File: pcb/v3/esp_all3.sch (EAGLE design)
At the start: 31 parts, among them IC1 4000D, Q1 BUZ11BH

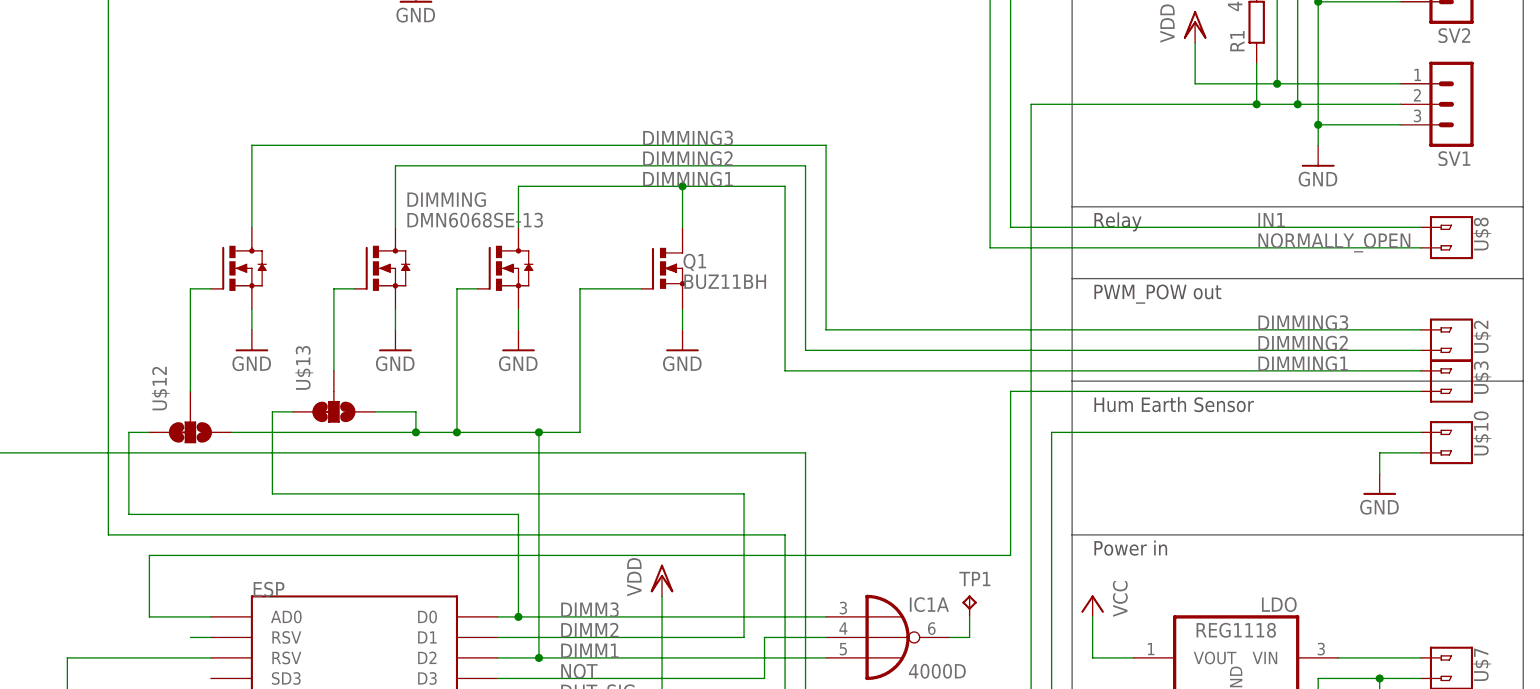
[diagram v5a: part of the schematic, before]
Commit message: added jumper
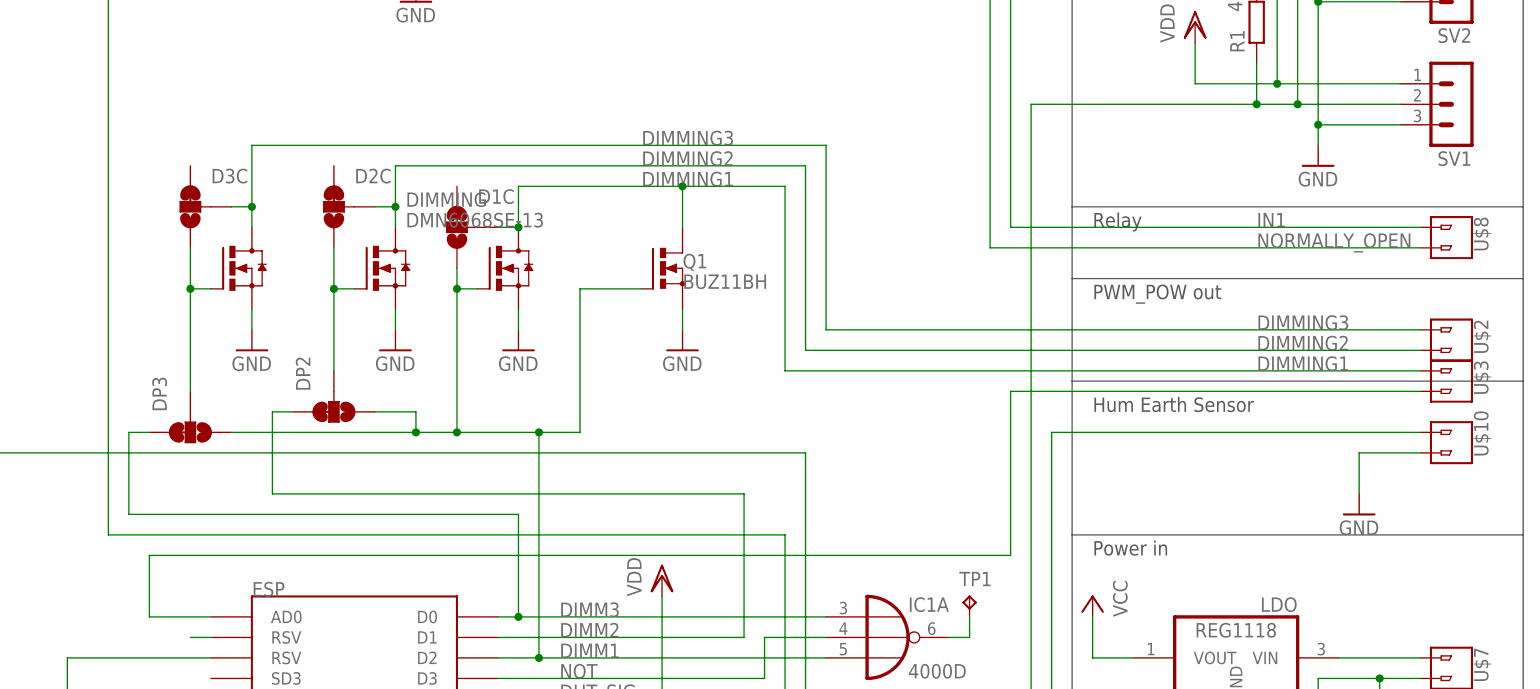
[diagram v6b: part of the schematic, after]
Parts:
- added D1C, D2C, D3C: SMD_SJ_3WAY_CLOSED, JKW_CHIP:SMD_SJ_3WAY_CLOSED
- renumbered U$12 to DP3, U$13 to DP2
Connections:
- net DIMM1: now also D1C.3
- net DIMMING1: now also D1C.2
- net DIMMING2: now also D2C.2
- net DIMMING3: now also D3C.2
- net N$20: now also D3C.3
- net N$21: now also D2C.3
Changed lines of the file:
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@@
 <part name="GND5" library="supply1" deviceset="GND" device=""/>
 <part name="U$10" library="JKW_CHIP" deviceset="2_PIN_CONNECTOR" device="" value="V1"/>
-<part name="GND6" library="supply1" deviceset="GND" device=""/>
 <part name="DHT22" library="diy-modules" deviceset="TEMP-HUM-SENSOR-DHT22" device=""/>
 <part name="SV1" library="con-lstb" deviceset="MA03-1" device=""/>
@@
 <part name="GND10" library="supply1" deviceset="GND" device=""/>
 <part name="GND12" library="supply1" deviceset="GND" device=""/>
-<part name="U$12" library="JKW_CHIP" deviceset="SMD_SJ_3WAY_CLOSED" device=""/>
-<part name="U$13" library="JKW_CHIP" deviceset="SMD_SJ_3WAY_CLOSED" device=""/>
+<part name="DP3" library="JKW_CHIP" deviceset="SMD_SJ_3WAY_CLOSED" device=""/>
+<part name="DP2" library="JKW_CHIP" deviceset="SMD_SJ_3WAY_CLOSED" device=""/>
 <part name="IC1" library="40xx" deviceset="4000" device="D"/>
 <part name="VDD5" library="supply1" deviceset="VDD" device=""/>
@@
 <part name="VDD6" library="supply1" deviceset="VDD" device=""/>
 <part name="VDD7" library="supply1" deviceset="VDD" device=""/>
+<part name="D3C" library="JKW_CHIP" deviceset="SMD_SJ_3WAY_CLOSED" device=""/>
+<part name="D2C" library="JKW_CHIP" deviceset="SMD_SJ_3WAY_CLOSED" device=""/>
+<part name="D1C" library="JKW_CHIP" deviceset="SMD_SJ_3WAY_CLOSED" device=""/>
+<part name="GND6" library="supply1" deviceset="GND" device=""/>
 </parts>
 <sheets>
@@
 <attribute name="NAME" x="216.662" y="83.312" size="1.778" layer="95" rot="R90"/>
 </instance>
-<instance part="GND6" gate="1" x="203.2" y="78.74"/>
 <instance part="DHT22" gate="G$1" x="-15.24" y="48.26" smashed="yes" rot="MR0">
 <attribute name="NAME" x="-25.4" y="63.5" size="1.778" layer="95" rot="MR180"/>
@@
 <instance part="GND10" gate="1" x="81.28" y="96.52"/>
 <instance part="GND12" gate="1" x="63.5" y="96.52"/>
-<instance part="U$12" gate="G$1" x="55.88" y="86.36" smashed="yes" rot="MR270">
+<instance part="DP3" gate="G$1" x="55.88" y="86.36" smashed="yes" rot="MR270">
 <attribute name="NAME" x="51.181" y="88.9" size="1.778" layer="95" rot="MR90"/>
 </instance>
-<instance part="U$13" gate="G$1" x="73.66" y="88.9" smashed="yes" rot="MR270">
+<instance part="DP2" gate="G$1" x="73.66" y="88.9" smashed="yes" rot="MR270">
 <attribute name="NAME" x="68.961" y="91.44" size="1.778" layer="95" rot="MR90"/>
 </instance>
@@
 <instance part="VDD6" gate="G$1" x="104.14" y="33.02"/>
 <instance part="VDD7" gate="G$1" x="114.3" y="68.58"/>
+<instance part="D3C" gate="G$1" x="55.88" y="114.3" smashed="yes" rot="MR0">
+<attribute name="NAME" x="58.42" y="118.999" size="1.778" layer="95" rot="MR180"/>
+</instance>
+<instance part="D2C" gate="G$1" x="73.66" y="114.3" smashed="yes" rot="MR0">
+<attribute name="NAME" x="76.2" y="118.999" size="1.778" layer="95" rot="MR180"/>
+</instance>
+<instance part="D1C" gate="G$1" x="88.9" y="111.76" smashed="yes" rot="MR0">
+<attribute name="NAME" x="91.44" y="116.459" size="1.778" layer="95" rot="MR180"/>
+</instance>
+<instance part="GND6" gate="1" x="200.66" y="76.2"/>
 </instances>
 <busses>
@@
 <wire x1="104.14" y1="86.36" x2="99.06" y2="86.36" width="0.1524" layer="91"/>
 <junction x="99.06" y="86.36"/>
-<pinref part="U$12" gate="G$1" pin="3"/>
+<pinref part="DP3" gate="G$1" pin="3"/>
 <wire x1="60.96" y1="86.36" x2="83.82" y2="86.36" width="0.1524" layer="91"/>
-<pinref part="U$13" gate="G$1" pin="3"/>
+<pinref part="DP2" gate="G$1" pin="3"/>
 <wire x1="83.82" y1="86.36" x2="88.9" y2="86.36" width="0.1524" layer="91"/>
 <wire x1="78.74" y1="88.9" x2="83.82" y2="88.9" width="0.1524" layer="91"/>
@@
 <junction x="99.06" y="58.42"/>
 <label x="101.6" y="58.42" size="1.778" layer="95"/>
+<pinref part="D1C" gate="G$1" pin="3"/>
+<wire x1="88.9" y1="106.68" x2="88.9" y2="104.14" width="0.1524" layer="91"/>
+<junction x="88.9" y="104.14"/>
 </segment>
 </net>
@@
 <wire x1="96.52" y1="76.2" x2="48.26" y2="76.2" width="0.1524" layer="91"/>
 <wire x1="48.26" y1="76.2" x2="48.26" y2="86.36" width="0.1524" layer="91"/>
-<pinref part="U$12" gate="G$1" pin="1"/>
+<pinref part="DP3" gate="G$1" pin="1"/>
 <wire x1="48.26" y1="86.36" x2="50.8" y2="86.36" width="0.1524" layer="91"/>
 <pinref part="IC1" gate="A" pin="I0"/>
@@
 <pinref part="GND5" gate="1" pin="GND"/>
 <wire x1="-10.16" y1="78.74" x2="-10.16" y2="96.52" width="0.1524" layer="91"/>
-</segment>
-<segment>
-<pinref part="U$10" gate="G$1" pin="2"/>
-<pinref part="GND6" gate="1" pin="GND"/>
-<wire x1="208.28" y1="83.82" x2="203.2" y2="83.82" width="0.1524" layer="91"/>
-<wire x1="203.2" y1="83.82" x2="203.2" y2="81.28" width="0.1524" layer="91"/>
 </segment>
 <segment>
@@
 <wire x1="-20.32" y1="7.62" x2="-20.32" y2="10.16" width="0.1524" layer="91"/>
 </segment>
+<segment>
+<pinref part="U$10" gate="G$1" pin="2"/>
+<wire x1="208.28" y1="83.82" x2="200.66" y2="83.82" width="0.1524" layer="91"/>
+<wire x1="200.66" y1="83.82" x2="200.66" y2="78.74" width="0.1524" layer="91"/>
+<pinref part="GND6" gate="1" pin="GND"/>
+</segment>
 </net>
 <net name="VCC" class="0">
@@
 <junction x="116.84" y="116.84"/>
 <label x="187.96" y="93.98" size="1.778" layer="95"/>
+<pinref part="D1C" gate="G$1" pin="2"/>
+<wire x1="93.98" y1="111.76" x2="96.52" y2="111.76" width="0.1524" layer="91"/>
+<junction x="96.52" y="111.76"/>
 </segment>
 </net>
@@
 <wire x1="124.46" y1="78.74" x2="66.04" y2="78.74" width="0.1524" layer="91"/>
 <wire x1="66.04" y1="78.74" x2="66.04" y2="88.9" width="0.1524" layer="91"/>
-<pinref part="U$13" gate="G$1" pin="1"/>
+<pinref part="DP2" gate="G$1" pin="1"/>
 <wire x1="66.04" y1="88.9" x2="68.58" y2="88.9" width="0.1524" layer="91"/>
 <label x="101.6" y="60.96" size="1.778" layer="95"/>
@@
 <pinref part="DIMMING1" gate="G$1" pin="D"/>
 <wire x1="132.08" y1="119.38" x2="81.28" y2="119.38" width="0.1524" layer="91"/>
-<wire x1="81.28" y1="119.38" x2="81.28" y2="111.76" width="0.1524" layer="91"/>
+<wire x1="81.28" y1="119.38" x2="81.28" y2="114.3" width="0.1524" layer="91"/>
 <label x="111.76" y="119.38" size="1.778" layer="95"/>
 <label x="187.96" y="96.52" size="1.778" layer="95"/>
+<pinref part="D2C" gate="G$1" pin="2"/>
+<wire x1="81.28" y1="114.3" x2="81.28" y2="111.76" width="0.1524" layer="91"/>
+<wire x1="78.74" y1="114.3" x2="81.28" y2="114.3" width="0.1524" layer="91"/>
+<junction x="81.28" y="114.3"/>
 </segment>
 </net>
@@
 <pinref part="DIMMING2" gate="G$1" pin="D"/>
 <wire x1="134.62" y1="121.92" x2="63.5" y2="121.92" width="0.1524" layer="91"/>
-<wire x1="63.5" y1="121.92" x2="63.5" y2="111.76" width="0.1524" layer="91"/>
+<wire x1="63.5" y1="121.92" x2="63.5" y2="114.3" width="0.1524" layer="91"/>
 <label x="111.76" y="121.92" size="1.778" layer="95"/>
 <label x="187.96" y="99.06" size="1.778" layer="95"/>
+<pinref part="D3C" gate="G$1" pin="2"/>
+<wire x1="63.5" y1="114.3" x2="63.5" y2="111.76" width="0.1524" layer="91"/>
+<wire x1="60.96" y1="114.3" x2="63.5" y2="114.3" width="0.1524" layer="91"/>
+<junction x="63.5" y="114.3"/>
 </segment>
 </net>
@@
 <segment>
 <pinref part="DIMMING2" gate="G$1" pin="G"/>
-<pinref part="U$12" gate="G$1" pin="2"/>
+<pinref part="DP3" gate="G$1" pin="2"/>
 <wire x1="55.88" y1="104.14" x2="58.42" y2="104.14" width="0.1524" layer="91"/>
 <wire x1="55.88" y1="91.44" x2="55.88" y2="104.14" width="0.1524" layer="91"/>
+<pinref part="D3C" gate="G$1" pin="3"/>
+<wire x1="55.88" y1="109.22" x2="55.88" y2="104.14" width="0.1524" layer="91"/>
+<junction x="55.88" y="104.14"/>
 </segment>
 </net>
@@
 <segment>
 <pinref part="DIMMING1" gate="G$1" pin="G"/>
-<pinref part="U$13" gate="G$1" pin="2"/>
+<pinref part="DP2" gate="G$1" pin="2"/>
 <wire x1="73.66" y1="104.14" x2="76.2" y2="104.14" width="0.1524" layer="91"/>
 <wire x1="73.66" y1="93.98" x2="73.66" y2="104.14" width="0.1524" layer="91"/>
-</segment>
-</net>
+<pinref part="D2C" gate="G$1" pin="3"/>
+<wire x1="73.66" y1="109.22" x2="73.66" y2="104.14" width="0.1524" layer="91"/>
+<junction x="73.66" y="104.14"/>
+</segment>
+</net>

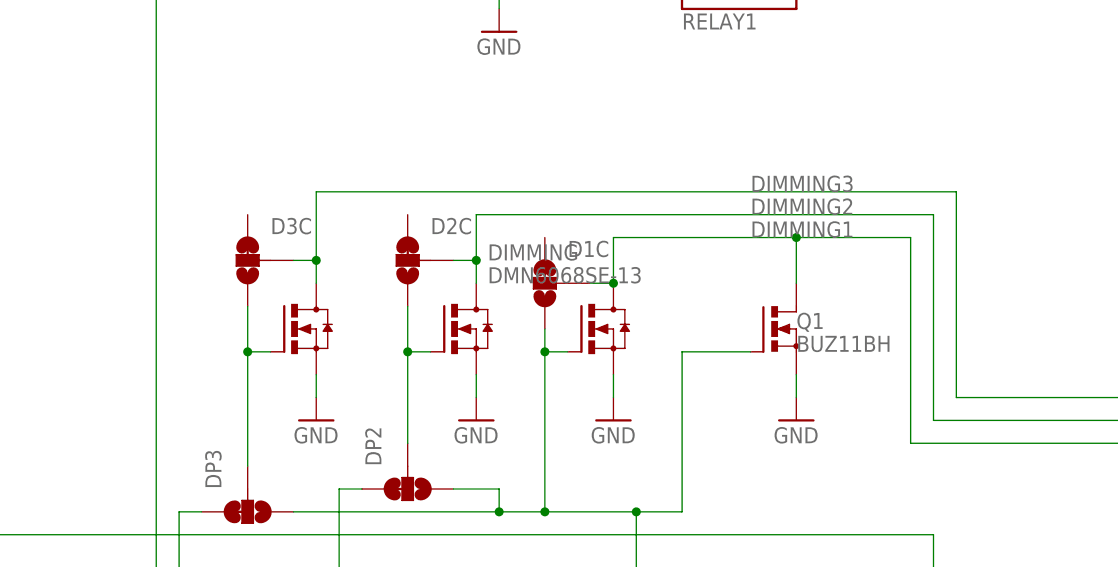
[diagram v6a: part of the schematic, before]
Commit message: added v4, with i2c
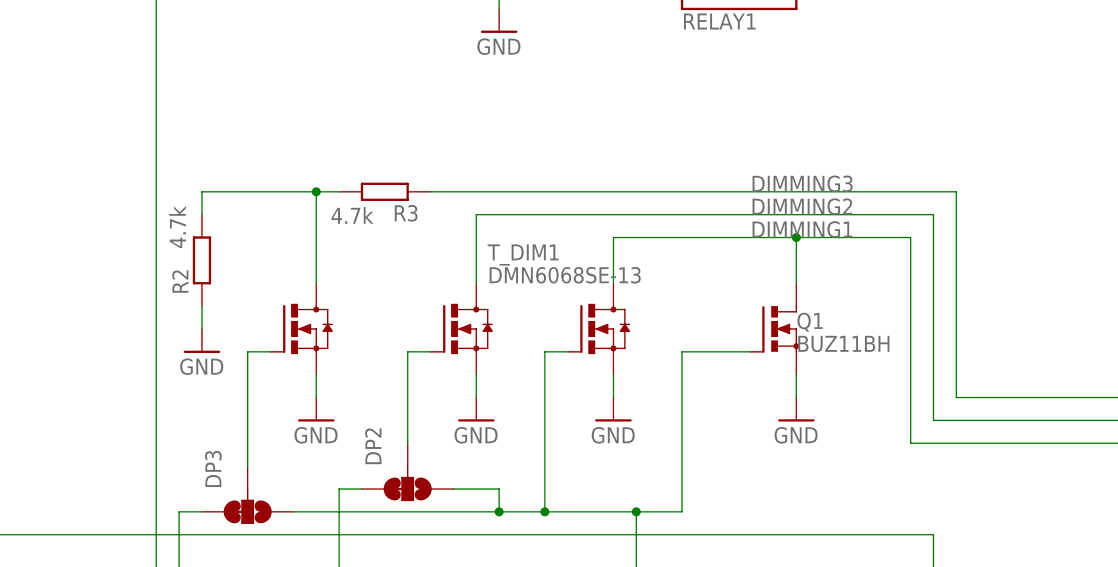
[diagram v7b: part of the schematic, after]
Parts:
- removed D1C, D2C, D3C: SMD_SJ_3WAY_CLOSED, JKW_CHIP:SMD_SJ_3WAY_CLOSED
- added R2, R3: 4.7k, rcl:R-EU_M0805
- renumbered DIMMING to T_DIM1, DIMMING1 to T_DIM2, DIMMING2 to T_DIM3
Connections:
- new net N$3: R2.2, R3.2, T_DIM3.D
- net DIMM1: no longer D1C.3
- net DIMMING1: no longer D1C.2
- net DIMMING2: no longer D2C.2
- net DIMMING3: now also R3.1; no longer D3C.2, T_DIM3.D
- net GND: now also R2.1
- net N$20: no longer D3C.3
- net N$21: no longer D2C.3
